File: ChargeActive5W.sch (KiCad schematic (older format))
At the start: 34 parts, among them Q2 IRLB3813PbF, Q3 IRLB3813PbF, U28 LM358

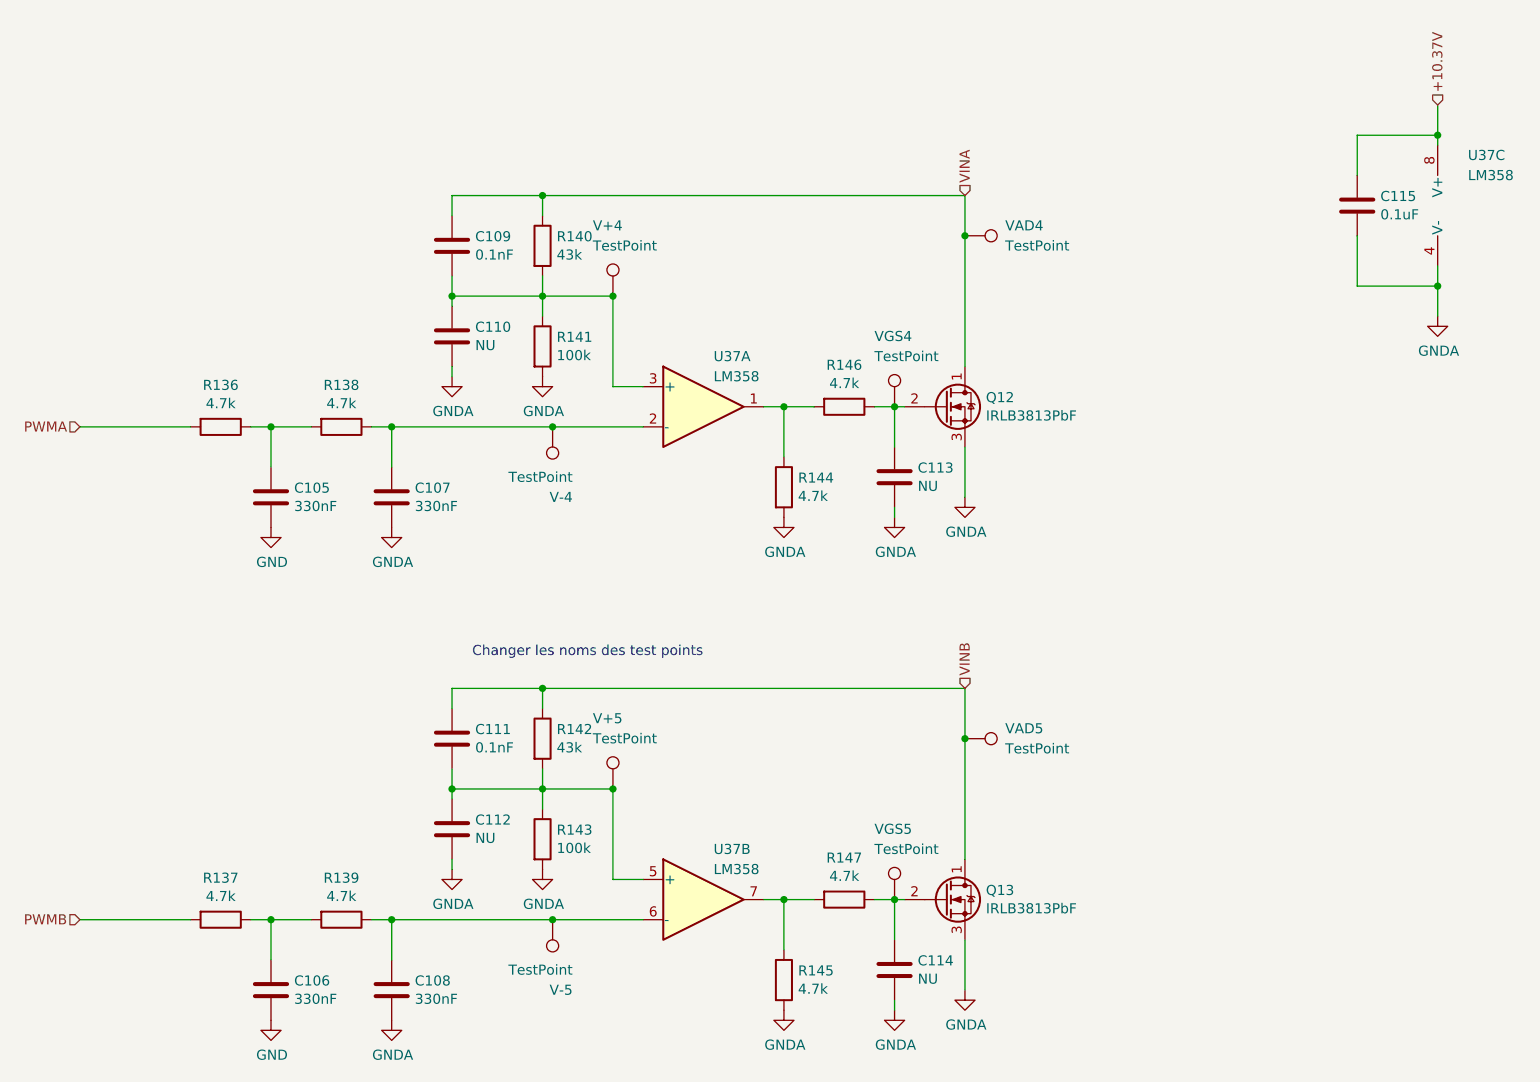
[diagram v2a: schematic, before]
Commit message: routing input canaux voltages
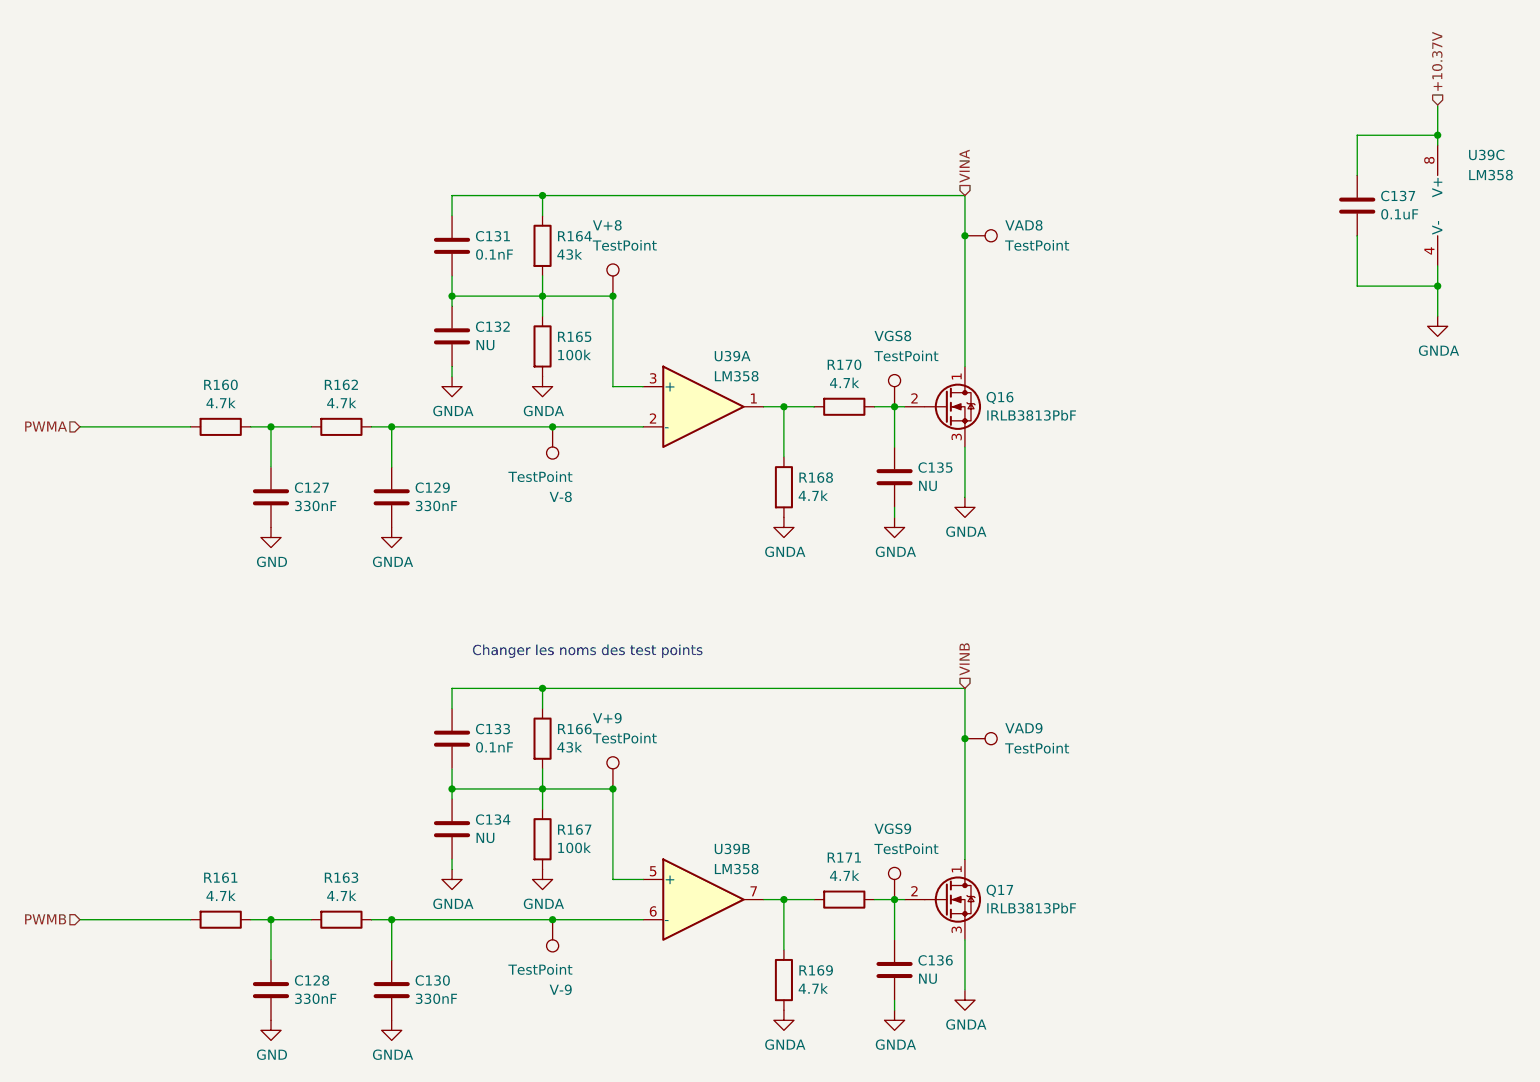
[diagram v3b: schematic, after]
